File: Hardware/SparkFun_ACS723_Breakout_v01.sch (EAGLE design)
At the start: 13 parts, among them U1 ACS712

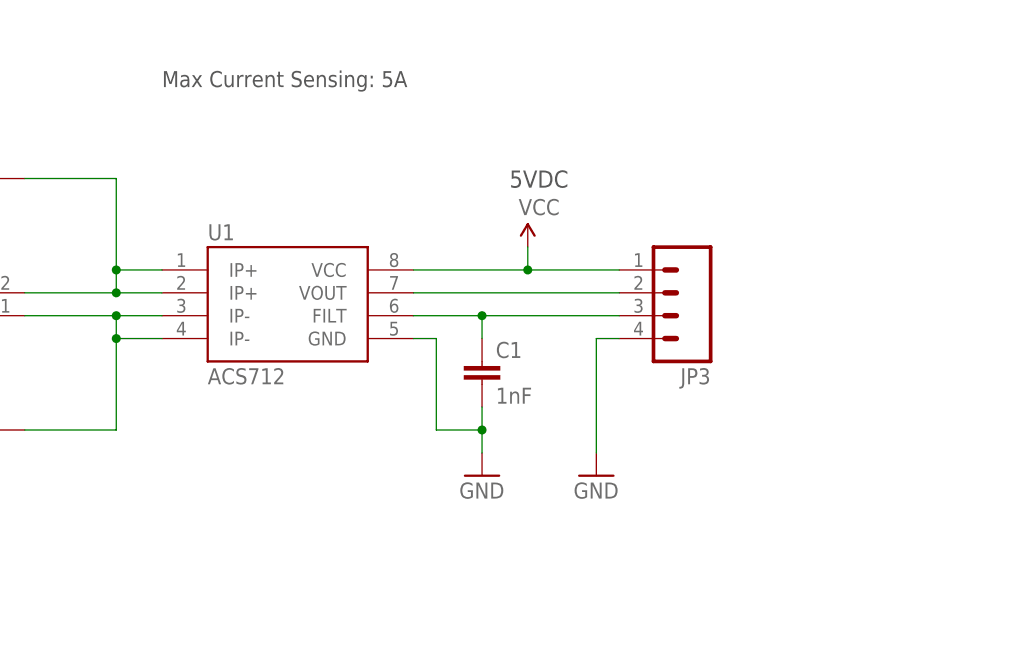
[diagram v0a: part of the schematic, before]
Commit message: removed old design and started new design
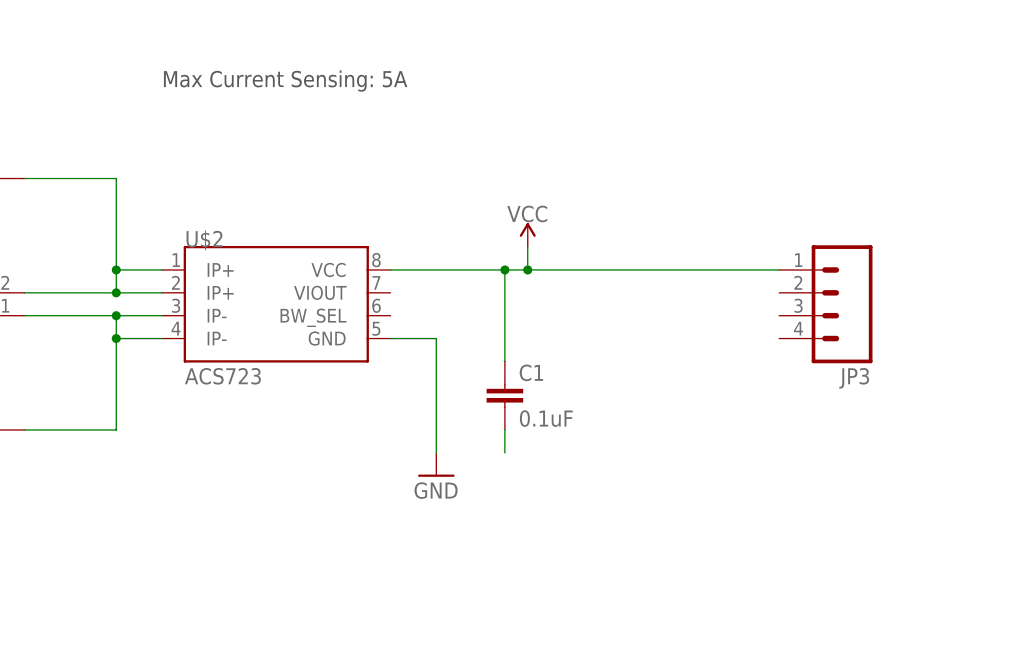
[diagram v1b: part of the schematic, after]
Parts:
- removed U1: ACS712, SparkFun-AnalogIC:ACS712
- added U$2: ACS723, SparkFun-IC-Power:ACS723
- C1: value 1nF -> 0.1uF; device SparkFun-Capacitors:1NF/1000PF-50V-10%(0603) -> SparkFun-Capacitors:0.1UF-0603-25V-(+80/-20%)
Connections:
- removed net FILT: C1.1, JP3.3, U1.FILT
- removed net GND: C1.2, JP3.4, U1.GND
- removed net VOUT: JP3.2, U1.VOUT
- new net N$1: C1.2
- net IP+: now also U$2.IP+@1, U$2.IP+@2; no longer U1.IP+@1, U1.IP+@2
- net IP-: now also U$2.IP-@1, U$2.IP-@2; no longer U1.IP-@3, U1.IP-@4
- net VCC: now also C1.1; no longer U1.VCC
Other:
- note removed: "5VDC"
- moved on the sheet: C1, JP3
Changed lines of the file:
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@@
 <?xml version="1.0" encoding="utf-8"?>
 <!DOCTYPE eagle SYSTEM "eagle.dtd">
-<eagle version="7.3.0">
+<eagle version="7.1.0">
 <drawing>
 <settings>
@@
 <layer number="112" name="tSilk" color="7" fill="1" visible="yes" active="yes"/>
 <layer number="113" name="IDFDebug" color="4" fill="1" visible="yes" active="yes"/>
+<layer number="114" name="Badge_Outline" color="7" fill="1" visible="yes" active="yes"/>
+<layer number="115" name="ReferenceISLANDS" color="7" fill="1" visible="yes" active="yes"/>
 <layer number="116" name="Patch_BOT" color="9" fill="4" visible="no" active="yes"/>
 <layer number="118" name="Rect_Pads" color="7" fill="1" visible="yes" active="yes"/>
@@
 <layer number="230" name="230bmp" color="7" fill="1" visible="yes" active="yes"/>
 <layer number="231" name="231bmp" color="7" fill="1" visible="yes" active="yes"/>
+<layer number="232" name="Eagle3D_PG2" color="7" fill="1" visible="yes" active="yes"/>
+<layer number="233" name="Eagle3D_PG3" color="7" fill="1" visible="yes" active="yes"/>
 <layer number="248" name="Housing" color="7" fill="1" visible="yes" active="yes"/>
 <layer number="249" name="Edge" color="7" fill="1" visible="yes" active="yes"/>
@@
 <layer number="255" name="routoute" color="7" fill="1" visible="yes" active="yes"/>
 </layers>
-<schematic xreflabel="%F%N/%S" xrefpart="/%S">
+<schematic xreflabel="%F%N/%S" xrefpart="/%S.%C%R">
 <attributes>
 </attributes>
@@
 <class number="0" name="default" width="0" drill="0">
 </class>
+<class number="1" name="8_mil" width="0.2032" drill="0">
+</class>
+<class number="2" name="10_mil" width="0.254" drill="0">
+</class>
+<class number="3" name="12_mil" width="0.3048" drill="0">
+</class>
+<class number="4" name="15_mil" width="0.381" drill="0">
+</class>
+<class number="5" name="20_mil" width="0.508" drill="0">
+</class>
+<class number="6" name="25_mil" width="0.635" drill="0">
+</class>
+<class number="7" name="30_mil" width="0.762" drill="0">
+</class>
 </classes>
 <parts>
-<part name="U1" library="SparkFun-AnalogIC" deviceset="ACS712" device=""/>
 <part name="FRAME1" library="SparkFun-Aesthetics" deviceset="FRAME-LETTER" device=""/>
 <part name="JP1" library="SparkFun-Connectors" deviceset="M01" device="-SMTSO-256-ET"/>
@@
 <part name="JP6" library="SparkFun-Connectors" deviceset="M02" device="1X02_NO_SILK"/>
 <part name="LOGO2" library="SparkFun-Aesthetics" deviceset="SFE_LOGO_FLAME" device=".3_INCH"/>
-<part name="C1" library="SparkFun-Capacitors" deviceset="1NF/1000PF-50V-10%(0603)" device="" value="1nF"/>
 <part name="LOGO1" library="SparkFun-Aesthetics" deviceset="SFE_LOGO_NAME" device=".1_INCH"/>
-<part name="SUPPLY1" library="SparkFun-Aesthetics" deviceset="VCC" device=""/>
+<part name="SUPPLY1" library="SparkFun-PowerSymbols" deviceset="VCC" device=""/>
 <part name="GND1" library="SparkFun-Aesthetics" deviceset="GND" device=""/>
-<part name="GND2" library="SparkFun-Aesthetics" deviceset="GND" device=""/>
 <part name="U$1" library="SparkFun-Aesthetics" deviceset="REVISION" device=""/>
+<part name="U$2" library="SparkFun-IC-Power" deviceset="ACS723" device=""/>
+<part name="C1" library="SparkFun-Capacitors" deviceset="0.1UF" device="-0603-25V-(+80/-20%)" value="0.1uF"/>
 </parts>
 <sheets>
@@
 <text x="170.18" y="11.43" size="2.54" layer="94">Pete Dokter</text>
 <text x="236.982" y="7.366" size="2.54" layer="94">V12</text>
-<text x="147.828" y="115.824" size="1.905" layer="97" font="vector" ratio="10">5VDC</text>
 <text x="173.99" y="6.604" size="2.54" layer="94">P. Alberts, Toni Klopfenstein</text>
 <text x="109.22" y="127" size="1.778" layer="97">Max Current Sensing: 5A</text>
 </plain>
 <instances>
-<instance part="U1" gate="G$1" x="124.46" y="101.6"/>
 <instance part="FRAME1" gate="G$1" x="0" y="0"/>
 <instance part="FRAME1" gate="V" x="147.32" y="0"/>
 <instance part="JP1" gate="G$1" x="86.36" y="116.84"/>
 <instance part="JP2" gate="G$1" x="86.36" y="88.9"/>
-<instance part="JP3" gate="G$1" x="165.1" y="104.14" rot="R180"/>
+<instance part="JP3" gate="G$1" x="182.88" y="104.14" rot="R180"/>
 <instance part="U$3" gate="G$1" x="236.22" y="45.72"/>
 <instance part="JP4" gate="G$1" x="246.38" y="25.4"/>
@@
 <instance part="JP6" gate="G$1" x="86.36" y="101.6"/>
 <instance part="LOGO2" gate="G$1" x="213.36" y="38.1"/>
-<instance part="C1" gate="G$1" x="144.78" y="93.98"/>
 <instance part="LOGO1" gate="G$1" x="149.86" y="35.56"/>
 <instance part="SUPPLY1" gate="G$1" x="149.86" y="109.22"/>
-<instance part="GND1" gate="1" x="144.78" y="83.82"/>
-<instance part="GND2" gate="1" x="157.48" y="83.82"/>
+<instance part="GND1" gate="1" x="139.7" y="83.82"/>
 <instance part="U$1" gate="G$1" x="149.098" y="6.858"/>
+<instance part="U$2" gate="G$1" x="121.92" y="101.6"/>
+<instance part="C1" gate="G$1" x="147.32" y="91.44"/>
 </instances>
 <busses>
@@
 <junction x="104.14" y="106.68"/>
 <pinref part="JP1" gate="G$1" pin="1"/>
-<pinref part="U1" gate="G$1" pin="IP+@1"/>
-<pinref part="U1" gate="G$1" pin="IP+@2"/>
 <pinref part="JP6" gate="G$1" pin="2"/>
 <wire x1="93.98" y1="104.14" x2="104.14" y2="104.14" width="0.1524" layer="91"/>
 <junction x="104.14" y="104.14"/>
+<pinref part="U$2" gate="G$1" pin="IP+@1"/>
+<pinref part="U$2" gate="G$1" pin="IP+@2"/>
 </segment>
 </net>
@@
 <wire x1="109.22" y1="99.06" x2="104.14" y2="99.06" width="0.1524" layer="91"/>
 <junction x="104.14" y="99.06"/>
-<pinref part="U1" gate="G$1" pin="IP-@3"/>
 <pinref part="JP2" gate="G$1" pin="1"/>
-<pinref part="U1" gate="G$1" pin="IP-@4"/>
 <pinref part="JP6" gate="G$1" pin="1"/>
 <wire x1="93.98" y1="101.6" x2="104.14" y2="101.6" width="0.1524" layer="91"/>
 <junction x="104.14" y="101.6"/>
+<pinref part="U$2" gate="G$1" pin="IP-@2"/>
+<pinref part="U$2" gate="G$1" pin="IP-@1"/>
 </segment>
 </net>
 <net name="VCC" class="0">
 <segment>
-<wire x1="137.16" y1="106.68" x2="149.86" y2="106.68" width="0.1524" layer="91"/>
-<pinref part="U1" gate="G$1" pin="VCC"/>
+<wire x1="134.62" y1="106.68" x2="147.32" y2="106.68" width="0.1524" layer="91"/>
+<wire x1="147.32" y1="106.68" x2="149.86" y2="106.68" width="0.1524" layer="91"/>
+<wire x1="149.86" y1="106.68" x2="149.86" y2="109.22" width="0.1524" layer="91"/>
+<pinref part="SUPPLY1" gate="G$1" pin="VCC"/>
+<pinref part="C1" gate="G$1" pin="1"/>
+<wire x1="147.32" y1="96.52" x2="147.32" y2="106.68" width="0.1524" layer="91"/>
+<junction x="147.32" y="106.68"/>
 <pinref part="JP3" gate="G$1" pin="1"/>
-<wire x1="149.86" y1="106.68" x2="160.02" y2="106.68" width="0.1524" layer="91"/>
-<wire x1="149.86" y1="106.68" x2="149.86" y2="109.22" width="0.1524" layer="91"/>
+<wire x1="149.86" y1="106.68" x2="177.8" y2="106.68" width="0.1524" layer="91"/>
 <junction x="149.86" y="106.68"/>
-<pinref part="SUPPLY1" gate="G$1" pin="VCC"/>
-</segment>
-</net>
-<net name="VOUT" class="0">
-<segment>
-<wire x1="160.02" y1="104.14" x2="137.16" y2="104.14" width="0.1524" layer="91"/>
-<pinref part="JP3" gate="G$1" pin="2"/>
-<pinref part="U1" gate="G$1" pin="VOUT"/>
-</segment>
-</net>
-<net name="FILT" class="0">
-<segment>
-<wire x1="137.16" y1="101.6" x2="144.78" y2="101.6" width="0.1524" layer="91"/>
-<pinref part="U1" gate="G$1" pin="FILT"/>
-<pinref part="JP3" gate="G$1" pin="3"/>
-<pinref part="C1" gate="G$1" pin="1"/>
-<wire x1="144.78" y1="101.6" x2="160.02" y2="101.6" width="0.1524" layer="91"/>
-<wire x1="144.78" y1="99.06" x2="144.78" y2="101.6" width="0.1524" layer="91"/>
-<junction x="144.78" y="101.6"/>
 </segment>
 </net>
 <net name="GND" class="0">
 <segment>
-<pinref part="U1" gate="G$1" pin="GND"/>
-<wire x1="137.16" y1="99.06" x2="139.7" y2="99.06" width="0.1524" layer="91"/>
-<wire x1="139.7" y1="99.06" x2="139.7" y2="88.9" width="0.1524" layer="91"/>
-<wire x1="139.7" y1="88.9" x2="144.78" y2="88.9" width="0.1524" layer="91"/>
-<wire x1="144.78" y1="88.9" x2="144.78" y2="91.44" width="0.1524" layer="91"/>
-<junction x="144.78" y="88.9"/>
+<wire x1="134.62" y1="99.06" x2="139.7" y2="99.06" width="0.1524" layer="91"/>
+<wire x1="139.7" y1="99.06" x2="139.7" y2="86.36" width="0.1524" layer="91"/>
+<pinref part="GND1" gate="1" pin="GND"/>
+</segment>
+</net>
+<net name="N$1" class="7">
+<segment>
 <pinref part="C1" gate="G$1" pin="2"/>
-<wire x1="144.78" y1="88.9" x2="144.78" y2="86.36" width="0.1524" layer="91"/>
-<pinref part="GND1" gate="1" pin="GND"/>
-</segment>
-<segment>
-<pinref part="JP3" gate="G$1" pin="4"/>
-<wire x1="160.02" y1="99.06" x2="157.48" y2="99.06" width="0.1524" layer="91"/>
-<wire x1="157.48" y1="99.06" x2="157.48" y2="86.36" width="0.1524" layer="91"/>
-<pinref part="GND2" gate="1" pin="GND"/>
-</segment>
-</net>
+<wire x1="147.32" y1="88.9" x2="147.32" y2="86.36" width="0.1524" layer="91"/>
+</segment>
+</net>
